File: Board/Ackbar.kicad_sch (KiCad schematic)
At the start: 15 parts, among them J1 TOF, J2 GNSS, J3 HALL, J4 MOTOR, J5 PWR_IN, J6 EPD, U1 ESP32-S3 Pico, U2 VREG, U3 TMC2209

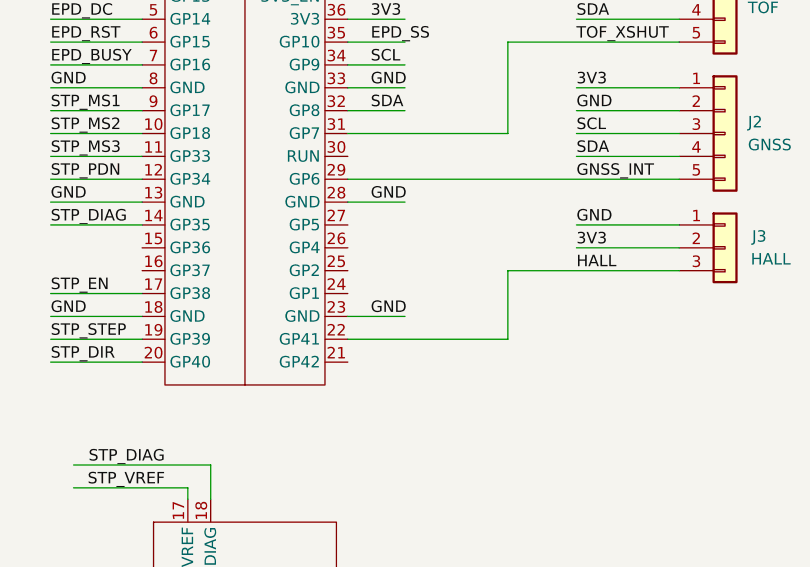
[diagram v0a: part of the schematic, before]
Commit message: Break out a few currently unused pins for config jumpers
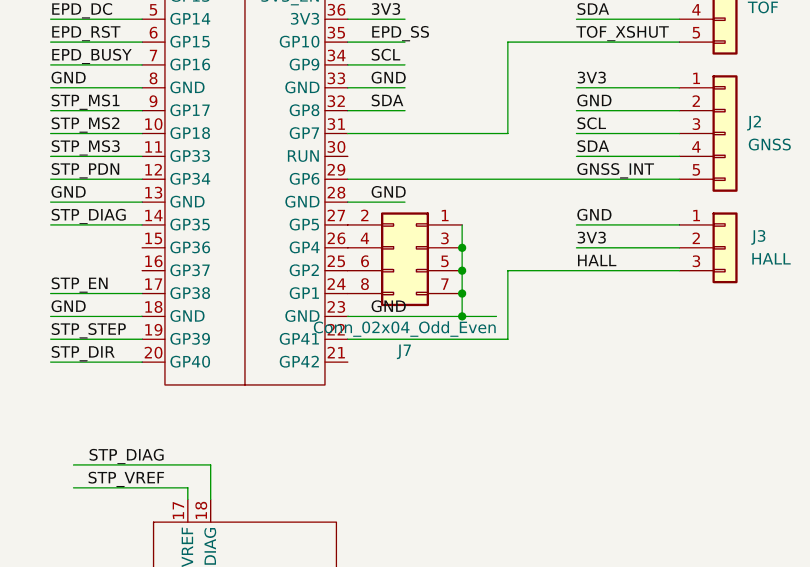
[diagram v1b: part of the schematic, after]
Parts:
- added J7: Conn_02x04_Odd_Even, Connector_PinSocket_2.54mm:PinSocket_2x04_P2.54mm_Vertical, symbol Connector_Generic:Conn_02x04_Odd_Even
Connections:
- net GND: now also J7.1 (Pin_1), J7.3 (Pin_3), J7.5 (Pin_5), J7.7 (Pin_7)
- net at U1.24 (GP1): now also J7.8 (Pin_8)
- net at U1.25 (GP2): now also J7.6 (Pin_6)
- net at U1.26 (GP4): now also J7.4 (Pin_4)
- net at U1.27 (GP5): now also J7.2 (Pin_2)
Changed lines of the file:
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@@
 (kicad_sch (version 20230121) (generator eeschema)
   (paper "A4")
+  (junction (at 135.89 81.28) (diameter 0) (color 0 0 0 0)
+  )
+  (junction (at 135.89 78.74) (diameter 0) (color 0 0 0 0)
+  )
+  (junction (at 135.89 83.82) (diameter 0) (color 0 0 0 0)
+  )
+  (junction (at 135.89 76.2) (diameter 0) (color 0 0 0 0)
+  )
   (wire (pts (xy 130.81 133.35) (xy 124.46 133.35))
     (stroke (width 0) (type default))
   )
+  (wire (pts (xy 123.19 68.58) (xy 160.02 68.58))
+    (stroke (width 0) (type default))
+  )
   (wire (pts (xy 105.41 102.87) (xy 105.41 104.14))
     (stroke (width 0) (type default))
@@
     (stroke (width 0) (type default))
   )
+  (wire (pts (xy 148.59 63.5) (xy 160.02 63.5))
+    (stroke (width 0) (type default))
+  )
+  (wire (pts (xy 148.59 58.42) (xy 160.02 58.42))
+    (stroke (width 0) (type default))
+  )
+  (wire (pts (xy 148.59 73.66) (xy 160.02 73.66))
+    (stroke (width 0) (type default))
+  )
+  (wire (pts (xy 140.97 78.74) (xy 160.02 78.74))
+    (stroke (width 0) (type default))
+  )
+  (wire (pts (xy 137.16 144.78) (xy 144.78 144.78))
+    (stroke (width 0) (type default))
+  )
+  (wire (pts (xy 90.17 48.26) (xy 100.33 48.26))
+    (stroke (width 0) (type default))
+  )
+  (wire (pts (xy 90.17 63.5) (xy 100.33 63.5))
+    (stroke (width 0) (type default))
+  )
+  (wire (pts (xy 99.06 128.27) (xy 92.71 128.27))
+    (stroke (width 0) (type default))
+  )
+  (wire (pts (xy 90.17 50.8) (xy 100.33 50.8))
+    (stroke (width 0) (type default))
+  )
+  (wire (pts (xy 86.36 125.73) (xy 99.06 125.73))
+    (stroke (width 0) (type default))
+  )
+  (wire (pts (xy 90.17 71.12) (xy 100.33 71.12))
+    (stroke (width 0) (type default))
+  )
+  (wire (pts (xy 86.36 123.19) (xy 86.36 120.65))
+    (stroke (width 0) (type default))
+  )
+  (wire (pts (xy 59.69 48.26) (xy 71.12 48.26))
+    (stroke (width 0) (type default))
+  )
+  (wire (pts (xy 123.19 147.32) (xy 129.54 147.32))
+    (stroke (width 0) (type default))
+  )
+  (wire (pts (xy 59.69 55.88) (xy 71.12 55.88))
+    (stroke (width 0) (type default))
+  )
+  (wire (pts (xy 90.17 45.72) (xy 100.33 45.72))
+    (stroke (width 0) (type default))
+  )
+  (wire (pts (xy 90.17 83.82) (xy 100.33 83.82))
+    (stroke (width 0) (type default))
+  )
+  (wire (pts (xy 90.17 55.88) (xy 100.33 55.88))
+    (stroke (width 0) (type default))
+  )
+  (wire (pts (xy 123.19 60.96) (xy 129.54 60.96))
+    (stroke (width 0) (type default))
+  )
+  (wire (pts (xy 123.19 63.5) (xy 140.97 63.5))
+    (stroke (width 0) (type default))
+  )
+  (wire (pts (xy 123.19 45.72) (xy 129.54 45.72))
+    (stroke (width 0) (type default))
+  )
+  (wire (pts (xy 135.89 73.66) (xy 135.89 76.2))
+    (stroke (width 0) (type default))
+  )
+  (wire (pts (xy 99.06 120.65) (xy 92.71 120.65))
+    (stroke (width 0) (type default))
+  )
+  (wire (pts (xy 90.17 73.66) (xy 100.33 73.66))
+    (stroke (width 0) (type default))
+  )
+  (wire (pts (xy 130.81 130.81) (xy 124.46 130.81))
+    (stroke (width 0) (type default))
+  )
+  (wire (pts (xy 123.19 43.18) (xy 129.54 43.18))
+    (stroke (width 0) (type default))
+  )
+  (wire (pts (xy 90.17 66.04) (xy 100.33 66.04))
+    (stroke (width 0) (type default))
+  )
+  (wire (pts (xy 140.97 53.34) (xy 160.02 53.34))
+    (stroke (width 0) (type default))
+  )
   (wire (pts (xy 123.19 71.12) (xy 129.54 71.12))
     (stroke (width 0) (type default))
   )
-  (wire (pts (xy 148.59 63.5) (xy 160.02 63.5))
-    (stroke (width 0) (type default))
-  )
-  (wire (pts (xy 123.19 68.58) (xy 160.02 68.58))
-    (stroke (width 0) (type default))
-  )
-  (wire (pts (xy 148.59 58.42) (xy 160.02 58.42))
-    (stroke (width 0) (type default))
-  )
-  (wire (pts (xy 148.59 73.66) (xy 160.02 73.66))
-    (stroke (width 0) (type default))
-  )
-  (wire (pts (xy 140.97 78.74) (xy 160.02 78.74))
-    (stroke (width 0) (type default))
-  )
-  (wire (pts (xy 137.16 144.78) (xy 144.78 144.78))
-    (stroke (width 0) (type default))
-  )
-  (wire (pts (xy 90.17 48.26) (xy 100.33 48.26))
-    (stroke (width 0) (type default))
-  )
-  (wire (pts (xy 90.17 63.5) (xy 100.33 63.5))
-    (stroke (width 0) (type default))
-  )
-  (wire (pts (xy 99.06 128.27) (xy 92.71 128.27))
-    (stroke (width 0) (type default))
-  )
-  (wire (pts (xy 90.17 50.8) (xy 100.33 50.8))
-    (stroke (width 0) (type default))
-  )
-  (wire (pts (xy 86.36 125.73) (xy 99.06 125.73))
-    (stroke (width 0) (type default))
-  )
-  (wire (pts (xy 90.17 71.12) (xy 100.33 71.12))
-    (stroke (width 0) (type default))
-  )
-  (wire (pts (xy 86.36 123.19) (xy 86.36 120.65))
-    (stroke (width 0) (type default))
-  )
-  (wire (pts (xy 59.69 48.26) (xy 71.12 48.26))
-    (stroke (width 0) (type default))
-  )
-  (wire (pts (xy 123.19 147.32) (xy 129.54 147.32))
-    (stroke (width 0) (type default))
-  )
-  (wire (pts (xy 59.69 55.88) (xy 71.12 55.88))
-    (stroke (width 0) (type default))
-  )
-  (wire (pts (xy 90.17 45.72) (xy 100.33 45.72))
-    (stroke (width 0) (type default))
-  )
-  (wire (pts (xy 90.17 83.82) (xy 100.33 83.82))
-    (stroke (width 0) (type default))
-  )
-  (wire (pts (xy 90.17 55.88) (xy 100.33 55.88))
-    (stroke (width 0) (type default))
-  )
-  (wire (pts (xy 123.19 60.96) (xy 129.54 60.96))
-    (stroke (width 0) (type default))
-  )
-  (wire (pts (xy 123.19 63.5) (xy 140.97 63.5))
-    (stroke (width 0) (type default))
-  )
-  (wire (pts (xy 123.19 45.72) (xy 129.54 45.72))
-    (stroke (width 0) (type default))
-  )
-  (wire (pts (xy 99.06 120.65) (xy 92.71 120.65))
-    (stroke (width 0) (type default))
-  )
-  (wire (pts (xy 90.17 73.66) (xy 100.33 73.66))
-    (stroke (width 0) (type default))
-  )
-  (wire (pts (xy 130.81 130.81) (xy 124.46 130.81))
-    (stroke (width 0) (type default))
-  )
-  (wire (pts (xy 123.19 43.18) (xy 129.54 43.18))
-    (stroke (width 0) (type default))
-  )
-  (wire (pts (xy 90.17 66.04) (xy 100.33 66.04))
-    (stroke (width 0) (type default))
-  )
-  (wire (pts (xy 140.97 53.34) (xy 160.02 53.34))
-    (stroke (width 0) (type default))
-  )
   (wire (pts (xy 59.69 53.34) (xy 71.12 53.34))
     (stroke (width 0) (type default))
@@
     (stroke (width 0) (type default))
   )
+  (wire (pts (xy 123.19 83.82) (xy 135.89 83.82))
+    (stroke (width 0) (type default))
+  )
   (wire (pts (xy 59.69 43.18) (xy 71.12 43.18))
     (stroke (width 0) (type default))
@@
     (stroke (width 0) (type default))
   )
+  (wire (pts (xy 135.89 81.28) (xy 135.89 83.82))
+    (stroke (width 0) (type default))
+  )
+  (wire (pts (xy 135.89 76.2) (xy 135.89 78.74))
+    (stroke (width 0) (type default))
+  )
   (wire (pts (xy 90.17 60.96) (xy 100.33 60.96))
     (stroke (width 0) (type default))
@@
     (stroke (width 0) (type default))
   )
+  (wire (pts (xy 135.89 78.74) (xy 135.89 81.28))
+    (stroke (width 0) (type default))
+  )
   (wire (pts (xy 129.54 144.78) (xy 129.54 147.32))
     (stroke (width 0) (type default))
@@
     (stroke (width 0) (type default))
   )
-  (wire (pts (xy 123.19 83.82) (xy 129.54 83.82))
-    (stroke (width 0) (type default))
-  )
   (wire (pts (xy 124.46 128.27) (xy 138.43 128.27))
+    (stroke (width 0) (type default))
+  )
+  (wire (pts (xy 135.89 83.82) (xy 139.7 83.82))
     (stroke (width 0) (type default))
   )
@@
         )
       )
+    )
+  )
+  (symbol (lib_id "Connector_Generic:Conn_02x04_Odd_Even") (at 130.81 76.2 0) (mirror y) (unit 1)
+    (in_bom yes) (on_board yes) (dnp no)
+    (property "Reference" "J7" (at 129.54 87.63 0)
+      (effects (font (size 1.27 1.27)))
+    )
+    (property "Value" "Conn_02x04_Odd_Even" (at 129.54 85.09 0)
+      (effects (font (size 1.27 1.27)))
+    )
+    (property "Footprint" "Connector_PinSocket_2.54mm:PinSocket_2x04_P2.54mm_Vertical" (at 130.81 76.2 0)
+      (effects (font (size 1.27 1.27)) hide)
+    )
+    (property "Datasheet" "~" (at 130.81 76.2 0)
+      (effects (font (size 1.27 1.27)) hide)
+    )
+    (pin "1")
+    (pin "2")
+    (pin "3")
+    (pin "4")
+    (pin "5")
+    (pin "6")
+    (pin "7")
+    (pin "8")
+    (instances
+      (project "Ackbar"
+        (path "/10d22af5-0d05-45a6-b4a8-43aad0d497f4"
+          (reference "J7") (unit 1)
+        )
+      )
